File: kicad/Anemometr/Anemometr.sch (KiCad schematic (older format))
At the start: 155 parts, among them J1 TxD, J10 +Z1, J11 +Z2, J12 +Z3, J13 +Z4, J14 -Z1, J15 -Z2, J16 -Z3, J17 -Z4, J18 1 TxD+, J19 2 TxD-, J2 RxD, J20 3 RxD+, J21 4-5, J22 6 RxD-, J23 7-8, J24 Conn_01x01_Female, J3 TMP117, J4 TMP117, J5 RST, J6 TMP117, J7 TMP117, J8 SWD, J9 SWC, Q1 5N10, U1 STM32F103C8Tx, U2 TS5A3166DBVR, U3 TS5A3166DBVR, U4 TS5A3166DBVR, U5 TS5A3166DBVR, U6 NCP1117-3.3, U7 MCP1700-5, U8 LMV7239, U9 MCP1700-3.3, Y1 8MHz, Y2 25MHz

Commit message: изменено:      Documents/circuit.png 	изменено:      kicad/Anemometr/Anemometr.kicad_pcb 	изменено:      kicad/Anemometr/Anemometr.pdf 	изменено:      kicad/Anemometr/Anemometr.sch 	изменено:      kicad/Anemometr/Anemometr.sch-bak 	изменено:      kicad/Anemometr/gerber/Anemometr-job.gbrjob 	изменено:      kicad/Anemometr/gerber/Border.gbr 	изменено:      kicad/Anemometr/gerber/Bottom.gbr 	изменено:      kicad/Anemometr/gerber/MaskBottom.gbr 	изменено:      kicad/Anemometr/gerber/MaskTop.gbr 	изменено:      kicad/Anemometr/gerber/NCData.drl 	изменено:      kicad/Anemometr/gerber/Top.gbr 	изменено:      kicad/Anemometr/gerber/anemometr.zip 	изменено:      kicad/Anemometr/gerber/mk-gerber.sh
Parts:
- added C59: 0.1, Capacitor_SMD:C_0603_1608Metric, symbol Device:C
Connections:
- net GND: now also C59.2
- net at R38.2, R39.1, U8.4 (-): now also C59.1
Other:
- moved on the sheet: C51, R38, R39, U8
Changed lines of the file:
@@
 L Connector:Conn_01x01_Female J24
 U 1 1 61CF9265
-P 11900 2000
-F 0 "J24" H 11928 1980 50  0001 L CNN
-F 1 "Conn_01x01_Female" H 11928 1935 50  0001 L CNN
-F 2 "My-library:SMD-CONN" H 11900 2000 50  0001 C CNN
-F 3 "~" H 11900 2000 50  0001 C CNN
-	1    11900 2000
+P 12050 2000
+F 0 "J24" H 12078 1980 50  0001 L CNN
+F 1 "Conn_01x01_Female" H 12078 1935 50  0001 L CNN
+F 2 "My-library:SMD-CONN" H 12050 2000 50  0001 C CNN
+F 3 "~" H 12050 2000 50  0001 C CNN
+	1    12050 2000
 	0    -1   -1   0
 $EndComp
@@
 L Device:C C51
 U 1 1 61CFA6DA
-P 11700 1650
-F 0 "C51" H 11850 1700 50  0000 L CNN
-F 1 "0.1uF" H 11850 1600 50  0000 L CNN
-F 2 "Capacitor_SMD:C_0603_1608Metric" H 11738 1500 50  0001 C CNN
-F 3 "~" H 11700 1650 50  0001 C CNN
-	1    11700 1650
+P 11850 1650
+F 0 "C51" H 12000 1700 50  0000 L CNN
+F 1 "0.1uF" H 12000 1600 50  0000 L CNN
+F 2 "Capacitor_SMD:C_0603_1608Metric" H 11888 1500 50  0001 C CNN
+F 3 "~" H 11850 1650 50  0001 C CNN
+	1    11850 1650
 	1    0    0    -1
 $EndComp
@@
 L power:GND #PWR068
 U 1 1 61CFAC14
-P 11700 1800
-F 0 "#PWR068" H 11700 1550 50  0001 C CNN
-F 1 "GND" H 11705 1627 50  0001 C CNN
-F 2 "" H 11700 1800 50  0001 C CNN
-F 3 "" H 11700 1800 50  0001 C CNN
-	1    11700 1800
+P 11850 1800
+F 0 "#PWR068" H 11850 1550 50  0001 C CNN
+F 1 "GND" H 11855 1627 50  0001 C CNN
+F 2 "" H 11850 1800 50  0001 C CNN
+F 3 "" H 11850 1800 50  0001 C CNN
+	1    11850 1800
 	1    0    0    -1
 $EndComp
@@
 L Comparator:MCP6566 U8
 U 1 1 61D85B4A
-P 11600 2200
-F 0 "U8" H 11550 2200 50  0000 L CNN
-F 1 "LMV7239" H 11650 2050 50  0000 L CNN
-F 2 "Package_TO_SOT_SMD:SOT-23-5" H 11600 1800 50  0001 C CNN
-F 3 "http://ww1.microchip.com/downloads/en/DeviceDoc/DS20002143E.pdf" H 11600 2200 50  0001 C CNN
-	1    11600 2200
+P 11750 2200
+F 0 "U8" H 11700 2200 50  0000 L CNN
+F 1 "LMV7239" H 11800 2050 50  0000 L CNN
+F 2 "Package_TO_SOT_SMD:SOT-23-5" H 11750 1800 50  0001 C CNN
+F 3 "http://ww1.microchip.com/downloads/en/DeviceDoc/DS20002143E.pdf" H 11750 2200 50  0001 C CNN
+	1    11750 2200
 	1    0    0    -1
 $EndComp
@@
 L Device:R R39
 U 1 1 61D8CCCE
-P 11250 2450
-F 0 "R39" H 11650 2450 50  0000 C CNN
-F 1 "10k" H 11650 2350 50  0000 C CNN
-F 2 "Resistor_SMD:R_0603_1608Metric" V 11180 2450 50  0001 C CNN
-F 3 "~" H 11250 2450 50  0001 C CNN
-	1    11250 2450
+P 11400 2450
+F 0 "R39" H 11800 2450 50  0000 C CNN
+F 1 "10k" H 11800 2350 50  0000 C CNN
+F 2 "Resistor_SMD:R_0603_1608Metric" V 11330 2450 50  0001 C CNN
+F 3 "~" H 11400 2450 50  0001 C CNN
+	1    11400 2450
 	1    0    0    -1
 $EndComp
 Wire Wire Line
-	11300 2300 11250 2300
+	11450 2300 11400 2300
 $Comp
 L Device:C C17
@@
 $EndComp
 Wire Wire Line
-	11100 2100 11300 2100
-Wire Wire Line
 	10800 2100 10800 1600
 Connection ~ 10800 2100
@@
 	1    0    0    -1
 $EndComp
-Text GLabel 11950 2200 2    50   Input ~ 0
+Text GLabel 12100 2200 2    50   Input ~ 0
 SensorInput
 Text GLabel 5800 4250 2    50   Input ~ 0
@@
 L power:+3.3V #PWR065
 U 1 1 61EE2066
-P 11250 1500
-F 0 "#PWR065" H 11250 1350 50  0001 C CNN
-F 1 "+3.3V" H 11265 1673 50  0000 C CNN
-F 2 "" H 11250 1500 50  0001 C CNN
-F 3 "" H 11250 1500 50  0001 C CNN
-	1    11250 1500
+P 11400 1500
+F 0 "#PWR065" H 11400 1350 50  0001 C CNN
+F 1 "+3.3V" H 11415 1673 50  0000 C CNN
+F 2 "" H 11400 1500 50  0001 C CNN
+F 3 "" H 11400 1500 50  0001 C CNN
+	1    11400 1500
 	1    0    0    -1
 $EndComp
@@
 	7650 2100 7650 2600
 Wire Wire Line
-	11950 2200 11900 2200
-Connection ~ 11900 2200
+	12100 2200 12050 2200
+Connection ~ 12050 2200
 Wire Wire Line
 	5800 4250 5750 4250
@@
 L Device:R R38
 U 1 1 61D8D3FA
-P 11250 1650
-F 0 "R38" H 11100 1700 50  0000 C CNN
-F 1 "100k" H 11100 1600 50  0000 C CNN
-F 2 "Resistor_SMD:R_0603_1608Metric" V 11180 1650 50  0001 C CNN
-F 3 "~" H 11250 1650 50  0001 C CNN
-	1    11250 1650
+P 11400 1650
+F 0 "R38" H 11250 1700 50  0000 C CNN
+F 1 "100k" H 11250 1600 50  0000 C CNN
+F 2 "Resistor_SMD:R_0603_1608Metric" V 11330 1650 50  0001 C CNN
+F 3 "~" H 11400 1650 50  0001 C CNN
+	1    11400 1650
 	1    0    0    -1
 $EndComp
 Wire Wire Line
-	11250 1800 11250 2300
+	11400 1800 11400 2300
 Wire Wire Line
-	11500 1500 11500 1900
-Connection ~ 11250 1500
+	11650 1500 11650 1900
+Connection ~ 11400 1500
 Wire Wire Line
-	11250 1500 11500 1500
+	11400 1500 11650 1500
 $Comp
 L power:+5VA #PWR053
@@
 Wire Wire Line
 	8500 2300 8650 2300
-Connection ~ 11250 2300
+Connection ~ 11400 2300
 Wire Wire Line
-	11500 2600 11250 2600
+	11650 2600 11400 2600
 Wire Wire Line
-	11500 2600 11500 2500
+	11650 2600 11650 2500
 Connection ~ 8300 2600
 Wire Wire Line
@@
 Wire Wire Line
 	9850 2600 8950 2600
-Connection ~ 11100 2600
 Wire Wire Line
 	11100 2600 9850 2600
-Connection ~ 11250 2600
+Connection ~ 11400 2600
 Wire Wire Line
-	11250 2600 11100 2600
+	11400 2600 11250 2600
 Wire Wire Line
 	11100 2300 11100 2100
-Connection ~ 11100 2100
 Wire Wire Line
 	9850 2300 9850 2200
@@
 $EndComp
 Wire Wire Line
-	11500 1500 11700 1500
-Connection ~ 11500 1500
+	11650 1500 11850 1500
+Connection ~ 11650 1500
 Wire Wire Line
 	9700 2000 10200 2000
@@
 Wire Wire Line
 	8950 1500 8950 2000
+$Comp
+L Device:C C59
+U 1 1 6254E96C
+P 11250 2450
+F 0 "C59" H 11250 2750 50  0000 L CNN
+F 1 "0.1" H 11250 2650 50  0000 L CNN
+F 2 "Capacitor_SMD:C_0603_1608Metric" H 11288 2300 50  0001 C CNN
+F 3 "~" H 11250 2450 50  0001 C CNN
+	1    11250 2450
+	1    0    0    -1
+$EndComp
+Wire Wire Line
+	11250 2300 11400 2300
+Wire Wire Line
+	11100 2100 11450 2100
+Connection ~ 11100 2100
+Wire Wire Line
+	11100 2600 11250 2600
+Connection ~ 11100 2600
+Connection ~ 11250 2600
 $EndSCHEMATC

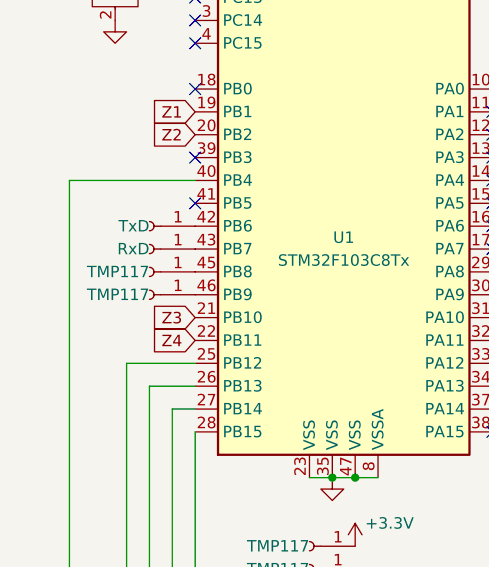
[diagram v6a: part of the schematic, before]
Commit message: изменено:      kicad/Anemometr/Anemometr.sch 	изменено:      kicad/Anemometr/Anemometr.sch-bak 	изменено:      kicad/TMP117/TMP117-cache.lib 	изменено:      kicad/TMP117/TMP117.sch 	изменено:      kicad/TMP117/TMP117.sch-bak 	изменено:      stm32cubeide/Anemometer/Core/Inc/main.h 	новый файл:    stm32cubeide/Anemometer/Core/Inc/tmp117.h 	изменено:      stm32cubeide/Anemometer/Core/Src/main.c 	новый файл:    stm32cubeide/Anemometer/Core/Src/tmp117.c 	изменено:      stm32cubeide/Anemometer/Release/Anemometer.bin 	изменено:      stm32cubeide/Anemometer/Release/Anemometer.elf 	изменено:      stm32cubeide/Anemometer/Release/Anemometer.list 	изменено:      stm32cubeide/Anemometer/Release/Anemometer.map 	изменено:      stm32cubeide/Anemometer/Release/Core/Src/main.d 	изменено:      stm32cubeide/Anemometer/Release/Core/Src/main.o 	изменено:      stm32cubeide/Anemometer/Release/Core/Src/main.su 	изменено:      stm32cubeide/Anemometer/Release/Core/Src/stm32f1xx_hal_msp.d 	изменено:      stm32cubeide/Anemometer/Release/Core/Src/stm32f1xx_hal_msp.o 	изменено:      stm32cubeide/Anemometer/Release/Core/Src/stm32f1xx_it.d 	изменено:      stm32cubeide/Anemometer/Release/Core/Src/stm32f1xx_it.o 	изменено:      stm32cubeide/Anemometer/Release/Core/Src/subdir.mk 	изменено:      stm32cubeide/Anemometer/Release/objects.list
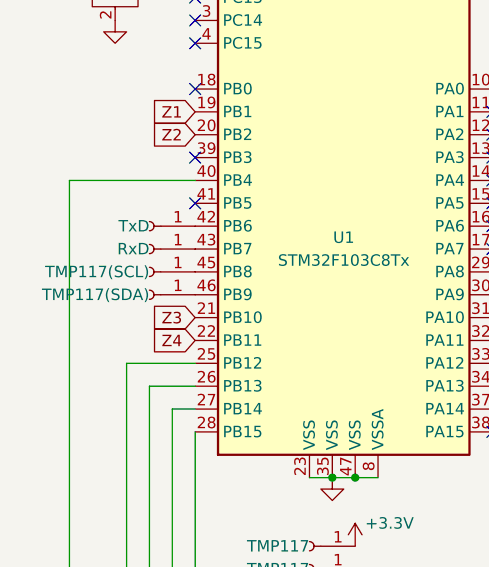
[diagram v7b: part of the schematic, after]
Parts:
- J3: value TMP117 -> TMP117(SCL)
- J4: value TMP117 -> TMP117(SDA)
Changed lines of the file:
@@
 P 4250 5050
 F 0 "J3" H 3750 5050 50  0001 C CNN
-F 1 "TMP117" H 4250 5050 50  0000 L CNN
+F 1 "TMP117(SCL)" H 4250 5050 50  0000 L CNN
 F 2 "My-library:SMD-CONN" H 4250 5050 50  0001 C CNN
 F 3 "~" H 4250 5050 50  0001 C CNN
@@
 P 4250 5150
 F 0 "J4" H 3750 5150 50  0001 C CNN
-F 1 "TMP117" H 4250 5150 50  0000 L CNN
+F 1 "TMP117(SDA)" H 4250 5150 50  0000 L CNN
 F 2 "My-library:SMD-CONN" H 4250 5150 50  0001 C CNN
 F 3 "~" H 4250 5150 50  0001 C CNN

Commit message: изменено:      all.zip 	изменено:      ../kicad/Anemometr/Anemometr.kicad_pcb 	изменено:      ../kicad/Anemometr/Anemometr.kicad_pcb-bak 	изменено:      ../kicad/Anemometr/Anemometr.sch 	изменено:      ../kicad/Anemometr/Anemometr.sch-bak 	удалено:       ../kicad/Anemometr/gerber/Anemometr-NPTH.drl 	изменено:      ../kicad/Anemometr/gerber/Anemometr-job.gbrjob 	изменено:      ../kicad/Anemometr/gerber/Border.gbr 	изменено:      ../kicad/Anemometr/gerber/Bottom.gbr 	изменено:      ../kicad/Anemometr/gerber/MaskBottom.gbr 	изменено:      ../kicad/Anemometr/gerber/MaskTop.gbr 	изменено:      ../kicad/Anemometr/gerber/NCData.drl 	изменено:      ../kicad/Anemometr/gerber/Top.gbr 	изменено:      ../kicad/Anemometr/gerber/anemometr.zip
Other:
- moved on the sheet: L1, Y1
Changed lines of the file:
@@
 	1    0    0    -1
 $EndComp
-Wire Wire Line
-	4250 3650 4450 3650
 $Comp
 L power:GND #PWR01
 U 1 1 61EF1494
-P 4100 3950
-F 0 "#PWR01" H 4100 3700 50  0001 C CNN
-F 1 "GND" H 4105 3777 50  0001 C CNN
-F 2 "" H 4100 3950 50  0001 C CNN
-F 3 "" H 4100 3950 50  0001 C CNN
-	1    4100 3950
+P 4200 3950
+F 0 "#PWR01" H 4200 3700 50  0001 C CNN
+F 1 "GND" H 4205 3777 50  0001 C CNN
+F 2 "" H 4200 3950 50  0001 C CNN
+F 3 "" H 4200 3950 50  0001 C CNN
+	1    4200 3950
 	1    0    0    -1
 $EndComp
@@
 $EndComp
 Wire Wire Line
-	4250 3650 4250 3750
-Wire Wire Line
-	4450 3550 3950 3550
-Wire Wire Line
-	3950 3550 3950 3750
+	4450 3550 4050 3550
 $Comp
 L Device:C C8
@@
 L Device:L L1
 U 1 1 622C7BCA
-P 6750 6350
-F 0 "L1" V 6940 6350 50  0000 C CNN
-F 1 "2.2uH" V 6849 6350 50  0000 C CNN
-F 2 "Inductor_SMD:L_0805_2012Metric" H 6750 6350 50  0001 C CNN
-F 3 "~" H 6750 6350 50  0001 C CNN
-	1    6750 6350
+P 6000 6550
+F 0 "L1" V 6190 6550 50  0000 C CNN
+F 1 "2.2uH" V 6099 6550 50  0000 C CNN
+F 2 "Inductor_SMD:L_0805_2012Metric" H 6000 6550 50  0001 C CNN
+F 3 "~" H 6000 6550 50  0001 C CNN
+	1    6000 6550
 	0    -1   -1   0
 $EndComp
@@
 L power:+3.3VA #PWR031
 U 1 1 622CB3E8
-P 6900 6350
-F 0 "#PWR031" H 6900 6200 50  0001 C CNN
-F 1 "+3.3VA" V 6850 6500 50  0000 L CNN
-F 2 "" H 6900 6350 50  0001 C CNN
-F 3 "" H 6900 6350 50  0001 C CNN
-	1    6900 6350
+P 6150 6550
+F 0 "#PWR031" H 6150 6400 50  0001 C CNN
+F 1 "+3.3VA" V 6100 6700 50  0000 L CNN
+F 2 "" H 6150 6550 50  0001 C CNN
+F 3 "" H 6150 6550 50  0001 C CNN
+	1    6150 6550
 	0    1    1    0
 $EndComp
@@
 U 1 1 629FD580
 P 11500 5300
-F 0 "D16" H 11900 5000 50  0000 C CNN
-F 1 "MBR0540" H 11900 5100 50  0000 C CNN
+F 0 "D16" H 11550 5000 50  0000 C CNN
+F 1 "MBR0540" H 11550 5100 50  0000 C CNN
 F 2 "Diode_SMD:D_SOD-123" H 11500 5300 50  0001 C CNN
 F 3 "~" H 11500 5300 50  0001 C CNN
@@
 L power:+3.3VDAC #PWR025
 U 1 1 627337E2
-P 6600 6350
-F 0 "#PWR025" H 6750 6300 50  0001 C CNN
-F 1 "+3.3VDAC" V 6620 6447 50  0000 L CNN
-F 2 "" H 6600 6350 50  0001 C CNN
-F 3 "" H 6600 6350 50  0001 C CNN
-	1    6600 6350
+P 5850 6550
+F 0 "#PWR025" H 6000 6500 50  0001 C CNN
+F 1 "+3.3VDAC" V 5870 6647 50  0000 L CNN
+F 2 "" H 5850 6550 50  0001 C CNN
+F 3 "" H 5850 6550 50  0001 C CNN
+	1    5850 6550
 	0    -1   -1   0
 $EndComp
@@
 L Device:Crystal_GND2 Y1
 U 1 1 62EA972F
-P 4100 3750
-F 0 "Y1" H 4100 4100 50  0000 C CNN
-F 1 "8MHz" H 4100 4000 50  0000 C CNN
-F 2 "Crystal:Resonator_SMD_muRata_CSTxExxV-3Pin_3.0x1.1mm" H 4100 3750 50  0001 C CNN
-F 3 "~" H 4100 3750 50  0001 C CNN
-	1    4100 3750
+P 4200 3750
+F 0 "Y1" H 4200 4100 50  0000 C CNN
+F 1 "8MHz" H 4200 4000 50  0000 C CNN
+F 2 "Crystal:Resonator_SMD_muRata_CSTxExxV-3Pin_3.0x1.1mm" H 4200 3750 50  0001 C CNN
+F 3 "~" H 4200 3750 50  0001 C CNN
+	1    4200 3750
 	1    0    0    -1
 $EndComp
@@
 Connection ~ 11100 2600
 Connection ~ 11250 2600
+Wire Wire Line
+	4350 3750 4350 3650
+Wire Wire Line
+	4350 3650 4450 3650
+Wire Wire Line
+	4050 3750 4050 3550
 $EndSCHEMATC
